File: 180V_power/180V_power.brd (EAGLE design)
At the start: 50 x 75 mm, 22 parts, among them IC1 NE555P, Q1 IRF740S, Q2 BC546

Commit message: new 180v board
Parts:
- L1: device iStivi - RCLD:0207/10 -> iStivi - RCLD:TFI0307
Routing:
- net N$10: track 15.5 -> 37.2 mm
- net N$6: track 62.7 -> 53.5 mm, vias 0 -> 1
- net N$3: track 34.3 -> 26.0 mm, vias 1 -> 0
- net N$26: track 96.5 -> 90.2 mm, vias 1 -> 0
- net N$1: track 24.3 -> 25.4 mm, vias 1 -> 0
- net N$4: track 13.9 -> 13.6 mm, vias 1 -> 0
- net N$5: track 26.4 -> 26.3 mm, vias 1 -> 0

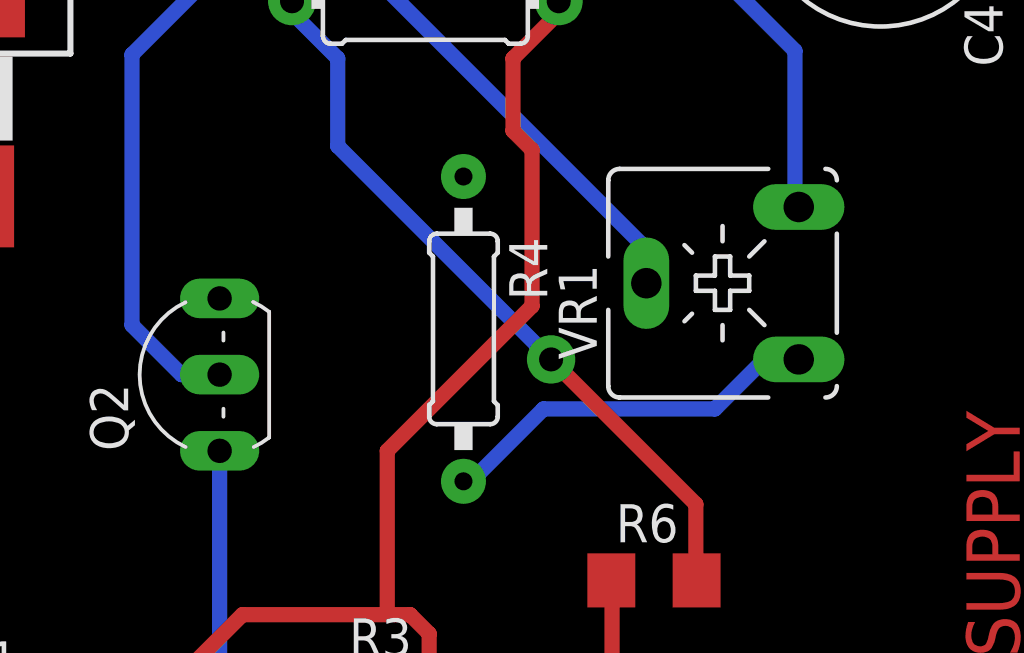
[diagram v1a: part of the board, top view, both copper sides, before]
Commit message: new 180V and tube tester
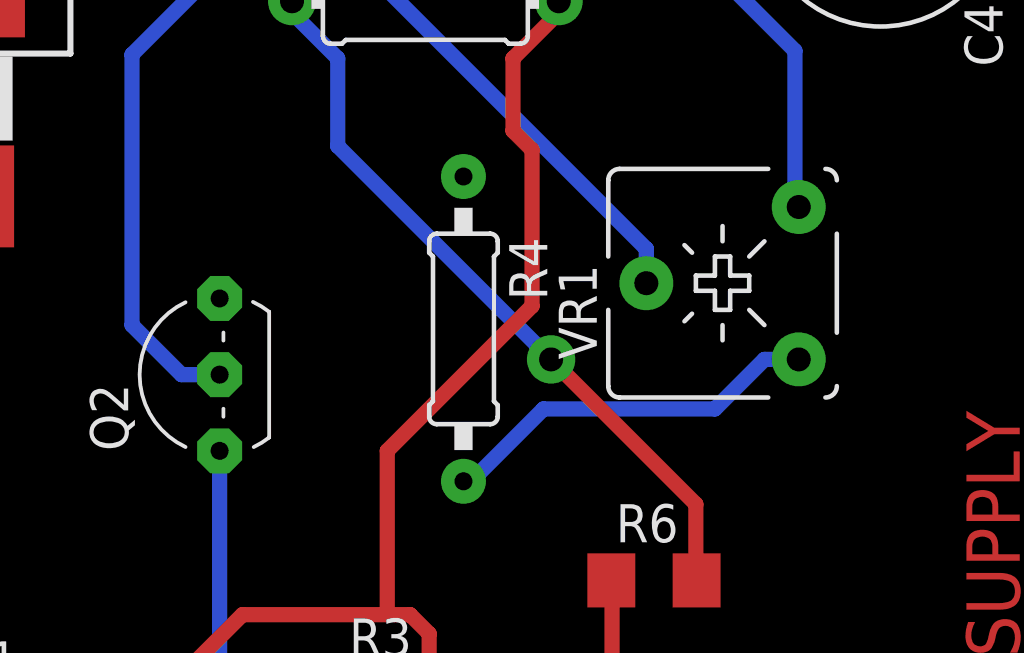
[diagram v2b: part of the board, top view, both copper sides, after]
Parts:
- Q2: device iStivi - Transistor-FET:TO92-EBC -> iStivi - Transistor-FET-reg:TO92-EBC
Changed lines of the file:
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@@
 <setting verticaltext="up"/>
 </settings>
-<grid distance="10" unitdist="mil" unit="mil" style="lines" multiple="1" display="no" altdistance="0.025" altunitdist="inch" altunit="inch"/>
+<grid distance="10" unitdist="mil" unit="mm" style="lines" multiple="1" display="no" altdistance="0.025" altunitdist="inch" altunit="inch"/>
 <layers>
 <layer number="1" name="Top" color="4" fill="1" visible="yes" active="yes"/>
@@
 <element name="R6" library="iStivi - RCLD" package="R1206" value="2K2" x="33.528" y="34.29"/>
 <element name="C3" library="iStivi - RCLD" package="C1206K" value="100pF" x="33.274" y="28.702"/>
-<element name="Q2" library="iStivi - Transistor-FET" package="TO92-EBC" value="BC546" x="17.78" y="41.148" rot="R90"/>
+<element name="Q2" library="iStivi - Transistor-FET-reg" package="TO92-EBC" value="BC546" x="17.78" y="41.148" rot="R90"/>
 <element name="C2" library="iStivi - RCLD" package="C1206K" value="2n2" x="33.274" y="24.638"/>
 <element name="L1" library="iStivi - RCLD" package="TFI0307" value="100uH" x="25.908" y="53.594"/>

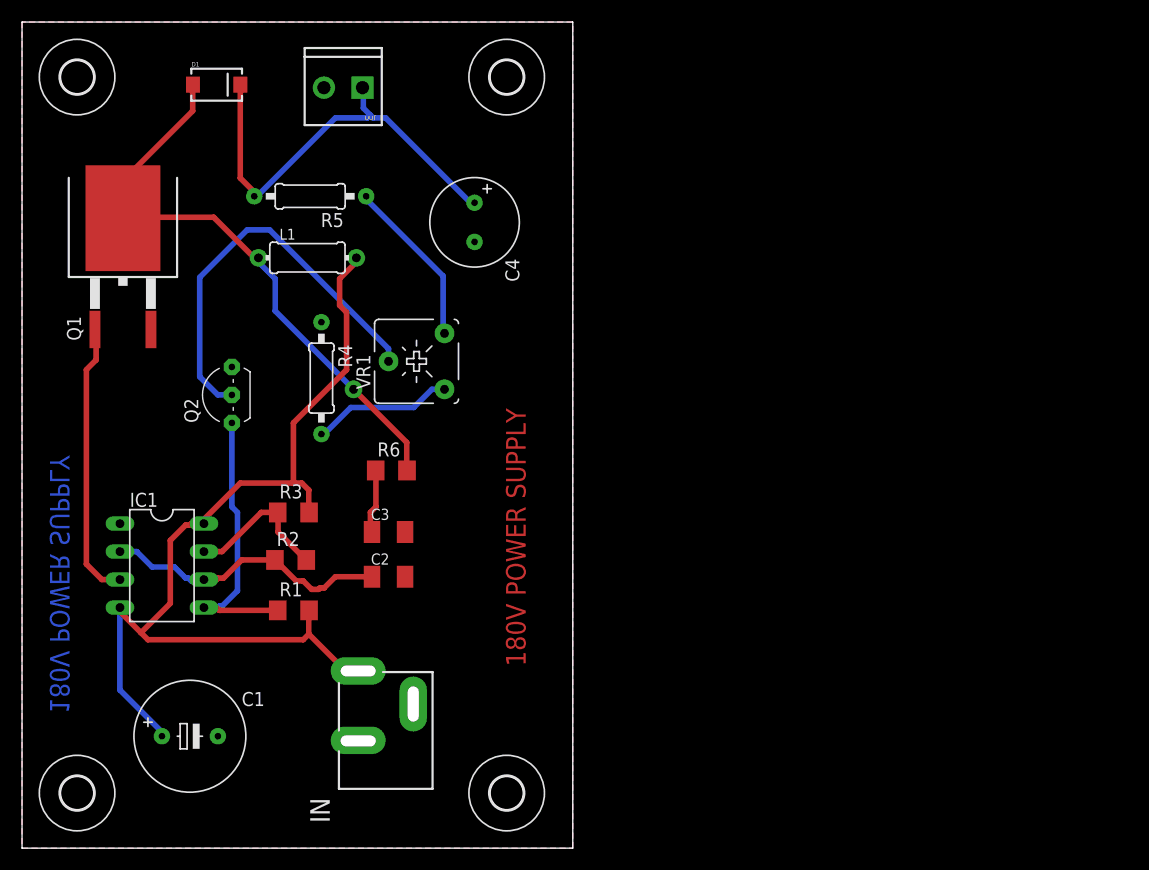
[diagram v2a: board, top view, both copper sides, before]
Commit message: new boards no cu pour
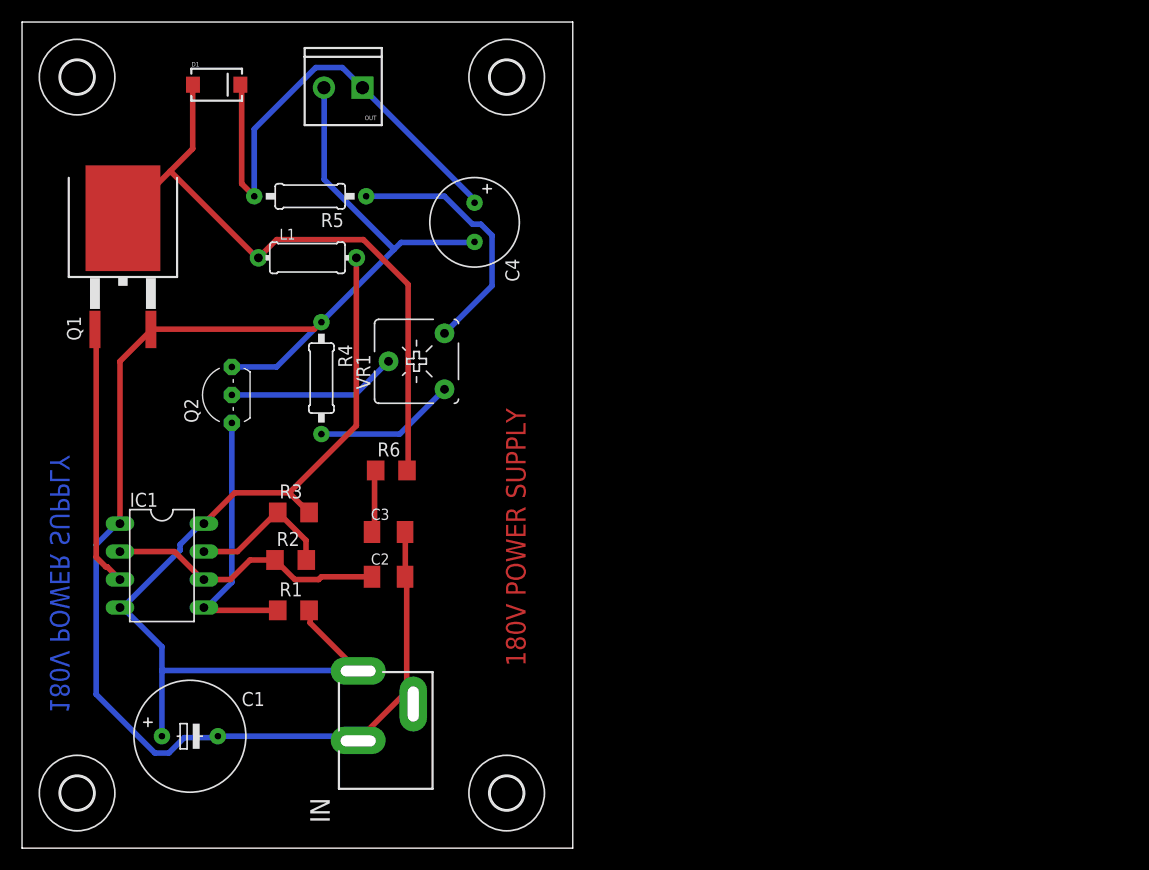
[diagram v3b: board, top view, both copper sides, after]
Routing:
- net GND: track 0.00 -> 145.2 mm
- net N$10: track 37.2 -> 15.5 mm
- net N$8: track 15.4 -> 23.6 mm
- net N$6: track 53.5 -> 59.0 mm, vias 1 -> 0
- net N$26: track 90.2 -> 85.0 mm
- net N$7: track 39.8 -> 44.3 mm
- net N$1: track 25.4 -> 23.7 mm
- net N$3: track 26.0 -> 24.8 mm
- net N$5: track 26.3 -> 25.5 mm
- removed copper zone on layer 1, net GND
- removed copper zone on layer 16, net GND

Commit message: new simple 180 board
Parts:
- removed IN: POWER_JACKSLT, iStivi - Header-Connector:POWER_JACK_SLOT
- added JP1: (no value), iStivi - Header-Connector:SCREWTERMINAL-3.5MM-2
- C2, C3: device iStivi - RCLD:C1206K -> iStivi - RCLD:C050-025X075
- D1: device iStivi - RCLD:SMA-DIODE -> iStivi - RCLD:DIODE-1N4001
- L1: value 100uH -> (none); device iStivi - RCLD:TFI0307 -> iStivi - RCLD:RBL0712
- Q1: value IRF740S -> IRF740; device iStivi - Transistor-FET:TO263 -> iStivi - Transistor-FET:TO220BV
- R1, R2, R3, R6: device iStivi - RCLD:R1206 -> iStivi - RCLD:0207/10
- moved OUT 76.3 mm to (76.2, 7.62), turned to 0 degrees
- moved D1 68.7 mm to (77.5, 35.6), turned to 270 degrees
- moved L1 63.1 mm to (85.1, 31.8), turned to 270 degrees
- moved U$3 56.4 mm to (94.0, 44.0)
- moved C4 51.5 mm to (77.5, 20.3), turned to 0 degrees
- moved R5 50.8 mm to (72.4, 38.1), turned to 270 degrees
- moved U$2 50.0 mm to (94.0, 6.00)
- moved Q2 48.0 mm to (63.5, 26.7), turned to 0 degrees
- moved IC1 40.7 mm to (52.1, 15.2), turned to 0 degrees
- moved R1 40.2 mm to (63.5, 31.8)
- moved Q1 33.6 mm to (40.6, 41.9)
- moved U$4 25.0 mm to (6.00, 45.0)
- moved C3 24.5 mm to (55.9, 38.1)
- moved R6 23.6 mm to (55.9, 41.9)
- moved R2 13.3 mm to (36.8, 21.6)
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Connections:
- net GND: now also JP1.2, Q1.S; no longer IN.GND@1, IN.GND@2, Q1.2
- net N$1: now also Q1.G; no longer Q1.1
- net N$26: now also JP1.1, L1.P$2; no longer IN.PWR, L1.2
- net N$6: now also L1.P$1, Q1.D; no longer L1.1, Q1.3
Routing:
- net N$26: track 85.0 -> 138.4 mm
- net N$10: track 15.5 -> 44.9 mm, vias 0 -> 2
- net N$8: track 23.6 -> 51.3 mm
- net GND: track 145.2 -> 172.0 mm, vias 0 -> 1
- net N$5: track 25.5 -> 49.1 mm
- net N$1: track 23.7 -> 43.9 mm, vias 0 -> 2
- net N$7: track 44.3 -> 29.2 mm
- net N$4: track 13.6 -> 23.5 mm
- net N$3: track 24.8 -> 15.8 mm
- net N$6: track 59.0 -> 52.3 mm
- net N$9: track 12.9 -> 14.2 mm
- net N$2: track 5.85 -> 4.86 mm
- added copper zone on layer 1, net GND
- added copper zone on layer 16, net GND
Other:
- board size 50 x 75 mm -> 100 x 50 mm
- board text removed: "100uH"
- board text removed: "180V"
- board text removed: "9-12V"
- board text removed: "GND"
- board text removed: "IRF740"
- board text removed: "NE555"
